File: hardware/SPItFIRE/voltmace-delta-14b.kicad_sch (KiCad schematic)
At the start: 17 parts

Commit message: The bulk of the schematic layout for the board (pending review and check)
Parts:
- renumbered 14B_L_SW10 to 14B_SW10L, 14B_M_SW10 to 14B_SW10M, 14B_R_SW10 to 14B_SW10R, 14B_X_RV0 to RV_X1, 14_B_Y_RV1 to RV_Y1

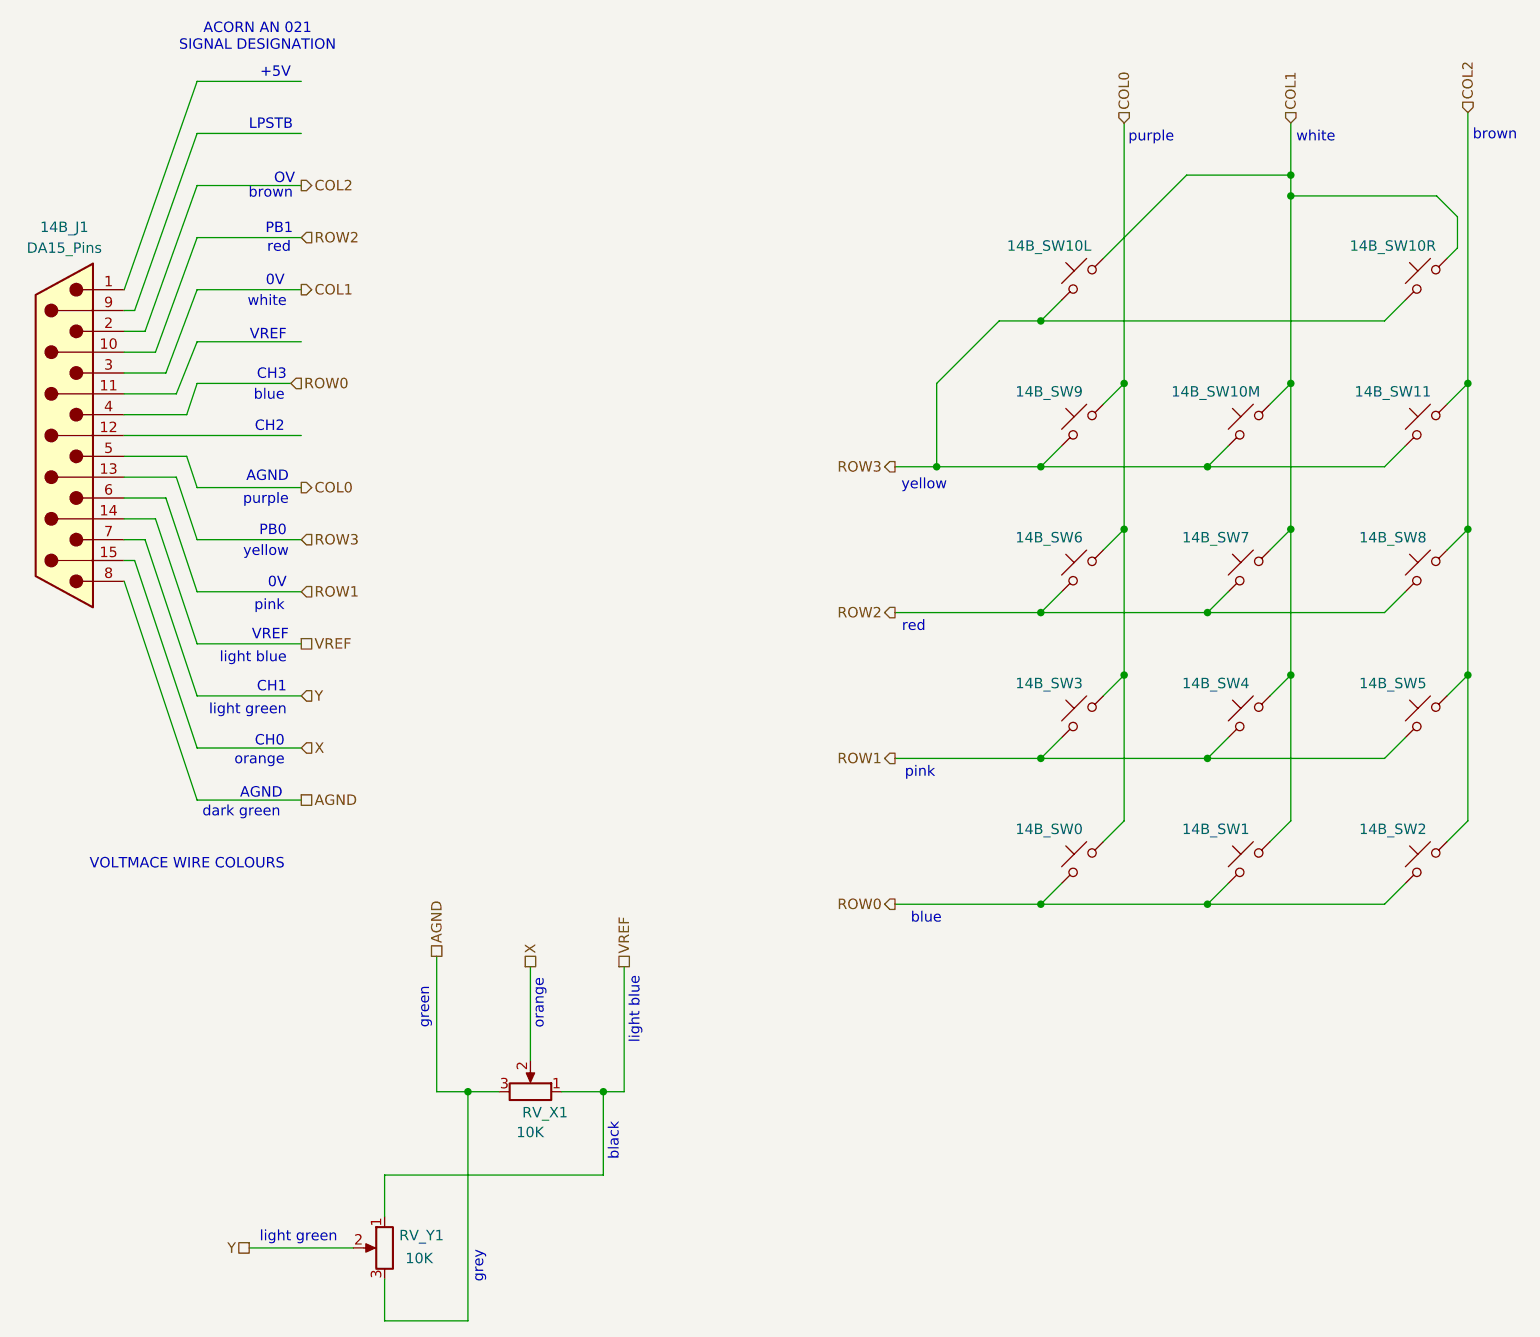
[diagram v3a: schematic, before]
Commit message: Schematic updates and rule checking
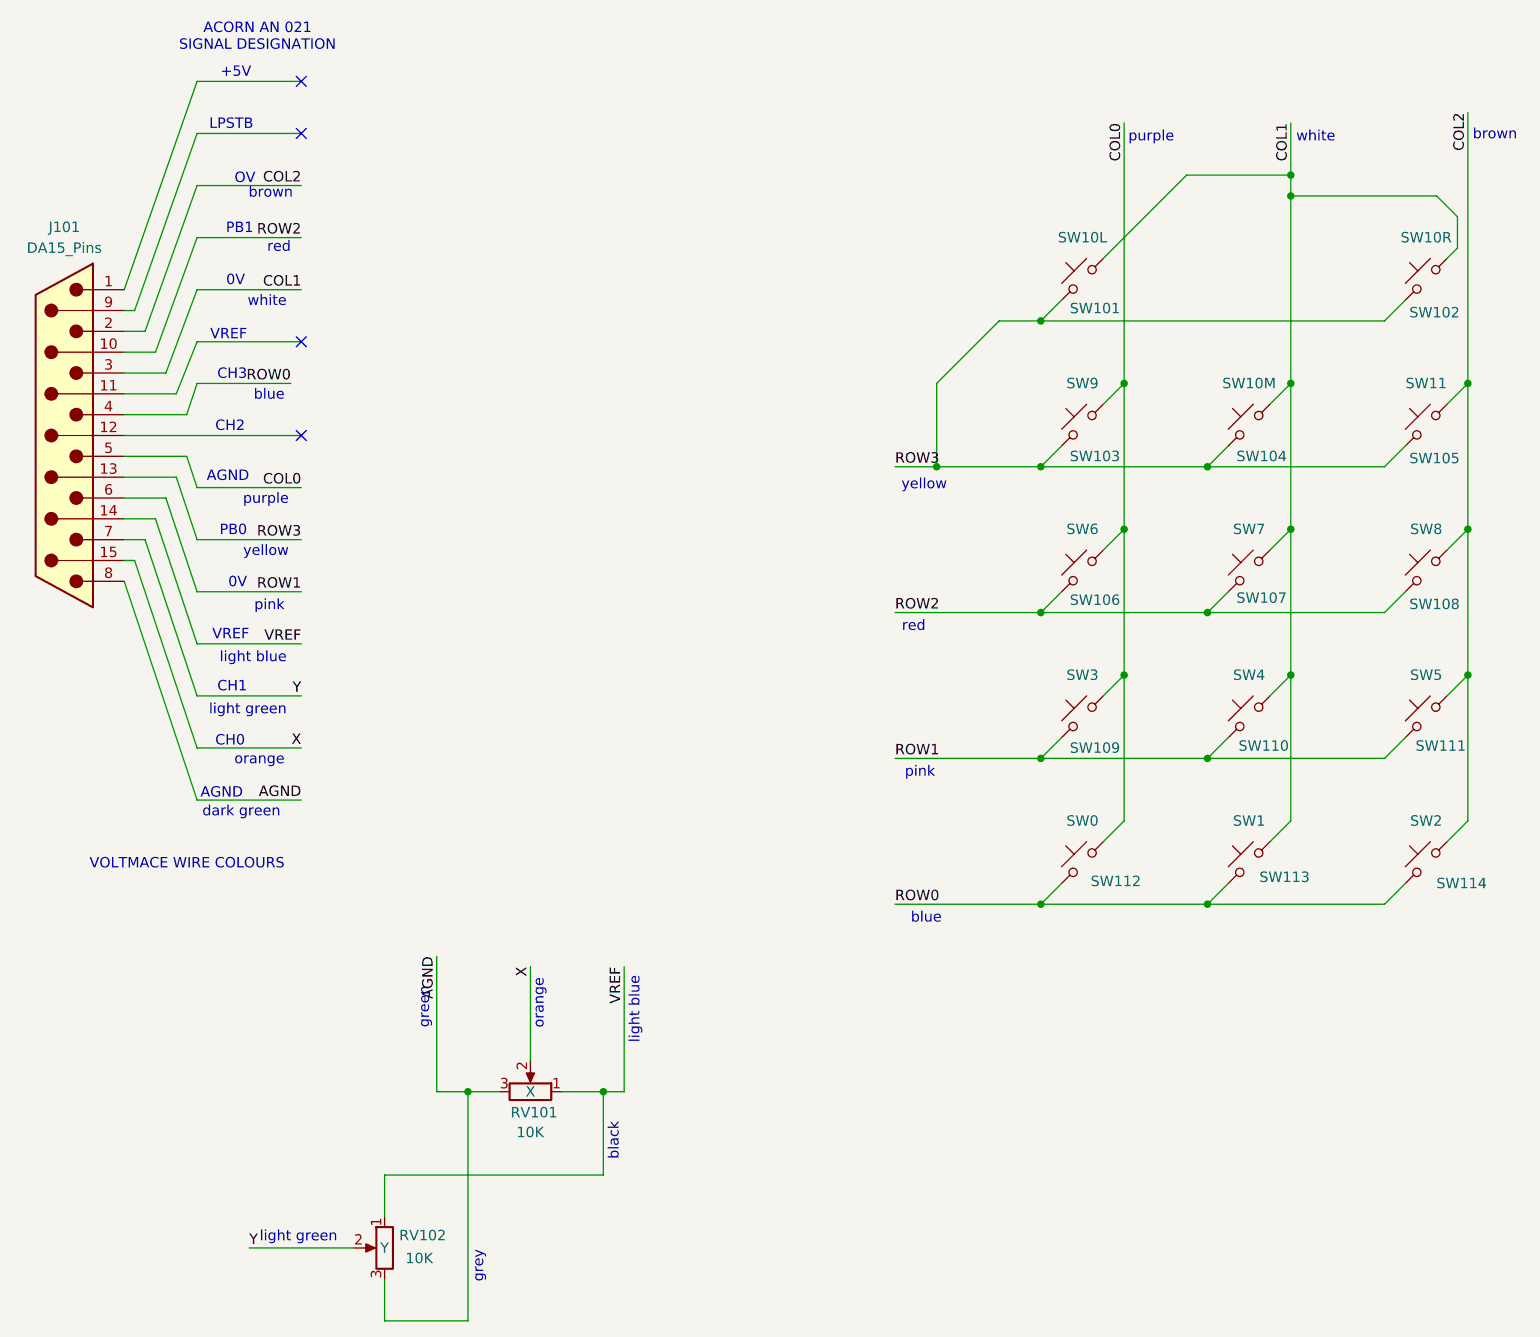
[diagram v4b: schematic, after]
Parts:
- RV101: renamed from RV_X1; Axis (none) -> X
- RV102: renamed from RV_Y1; Axis (none) -> Y
- SW101: renamed from 14B_SW10L; value SW_Push_45deg -> SW10L
- SW102: renamed from 14B_SW10R; value SW_Push_45deg -> SW10R
- SW103: renamed from 14B_SW9; value SW_Push_45deg -> SW9
- SW104: renamed from 14B_SW10M; value SW_Push_45deg -> SW10M
- SW105: renamed from 14B_SW11; value SW_Push_45deg -> SW11
- SW106: renamed from 14B_SW6; value SW_Push_45deg -> SW6
- SW107: renamed from 14B_SW7; value SW_Push_45deg -> SW7
- SW108: renamed from 14B_SW8; value SW_Push_45deg -> SW8
- SW109: renamed from 14B_SW3; value SW_Push_45deg -> SW3
- SW110: renamed from 14B_SW4; value SW_Push_45deg -> SW4
- SW111: renamed from 14B_SW5; value SW_Push_45deg -> SW5
- SW112: renamed from 14B_SW0; value SW_Push_45deg -> SW0
- SW113: renamed from 14B_SW1; value SW_Push_45deg -> SW1
- SW114: renamed from 14B_SW2; value SW_Push_45deg -> SW2
- renumbered 14B_J1 to J101
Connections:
- no-connect marks 0 -> 4
